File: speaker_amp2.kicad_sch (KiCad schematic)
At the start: 1 part

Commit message: refactored repo
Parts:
- removed MCU1: ESP32-C6-DevKit-N8, RF_Module:ESP32-C6-DevKit-N8, symbol RF_Module:ESP32-C6-DevKit-N8
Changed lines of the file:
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@@
 	(generator_version "8.0")
 	(paper "A4")
-	(symbol
-		(lib_id "RF_Module:ESP32-C6-DevKit-N8")
-		(at 93.98 91.44 0)
-		(unit 1)
-		(exclude_from_sim no)
-		(in_bom yes)
-		(on_board yes)
-		(dnp no)
-		(fields_autoplaced yes)
-		(property "Reference" "MCU1"
-			(at 93.98 45.72 0)
-			(effects
-				(font
-					(size 1.27 1.27)
-				)
-			)
-		)
-		(property "Value" "ESP32-C6-DevKit-N8"
-			(at 93.98 48.26 0)
-			(effects
-				(font
-					(size 1.27 1.27)
-				)
-			)
-		)
-		(property "Footprint" "RF_Module:ESP32-C6-DevKit-N8"
-			(at 93.98 78.74 0)
-			(effects
-				(font
-					(size 1.27 1.27)
-				)
-				(hide yes)
-			)
-		)
-		(property "Datasheet" "https://www.waveshare.com/wiki/ESP32-C6-DEV-KIT-N8"
-			(at 93.726 44.196 0)
-			(effects
-				(font
-					(size 1.27 1.27)
-				)
-				(hide yes)
-			)
-		)
-		(property "Description" ""
-			(at 93.98 78.74 0)
-			(effects
-				(font
-					(size 1.27 1.27)
-				)
-				(hide yes)
-			)
-		)
-		(pin "7"
-		)
-		(pin "25"
-		)
-		(pin "32"
-		)
-		(pin "26"
-		)
-		(pin "31"
-		)
-		(pin "30"
-		)
-		(pin "14"
-		)
-		(pin "21"
-		)
-		(pin "10"
-		)
-		(pin "19"
-		)
-		(pin "12"
-		)
-		(pin "27"
-		)
-		(pin "8"
-		)
-		(pin "20"
-		)
-		(pin "11"
-		)
-		(pin "16"
-		)
-		(pin "2"
-		)
-		(pin "4"
-		)
-		(pin "5"
-		)
-		(pin "3"
-		)
-		(pin "28"
-		)
-		(pin "23"
-		)
-		(pin "29"
-		)
-		(pin "24"
-		)
-		(pin "17"
-		)
-		(pin "15"
-		)
-		(pin "18"
-		)
-		(pin "13"
-		)
-		(pin "9"
-		)
-		(pin "22"
-		)
-		(pin "6"
-		)
-		(pin "1"
-		)
-		(instances
-			(project ""
-				(path "/2f0da60f-7f2b-417d-9b6a-7955d19177ea"
-					(reference "MCU1")
-					(unit 1)
-				)
-			)
-		)
-	)
 	(sheet_instances
 		(path "/"

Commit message: added mcu to schematic
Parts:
- added MCU1: ESP32-C6-DevKit-N8, Speaker Amp Lib:ESP32-C6-DevKit-N8, symbol Speaker Amp Lib:ESP32-C6-DevKit-N8
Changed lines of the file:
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@@
 	(generator_version "8.0")
 	(paper "A4")
+	(symbol
+		(lib_id "Speaker Amp Lib:ESP32-C6-DevKit-N8")
+		(at 83.82 93.98 0)
+		(unit 1)
+		(exclude_from_sim no)
+		(in_bom yes)
+		(on_board yes)
+		(dnp no)
+		(fields_autoplaced yes)
+		(property "Reference" "MCU1"
+			(at 83.82 48.26 0)
+			(effects
+				(font
+					(size 1.27 1.27)
+				)
+			)
+		)
+		(property "Value" "ESP32-C6-DevKit-N8"
+			(at 83.82 50.8 0)
+			(effects
+				(font
+					(size 1.27 1.27)
+				)
+			)
+		)
+		(property "Footprint" "Speaker Amp Lib:ESP32-C6-DevKit-N8"
+			(at 83.82 81.28 0)
+			(effects
+				(font
+					(size 1.27 1.27)
+				)
+				(hide yes)
+			)
+		)
+		(property "Datasheet" "https://www.waveshare.com/wiki/ESP32-C6-DEV-KIT-N8"
+			(at 83.566 46.736 0)
+			(effects
+				(font
+					(size 1.27 1.27)
+				)
+				(hide yes)
+			)
+		)
+		(property "Description" ""
+			(at 83.82 81.28 0)
+			(effects
+				(font
+					(size 1.27 1.27)
+				)
+				(hide yes)
+			)
+		)
+		(pin "22"
+		)
+		(pin "18"
+		)
+		(pin "9"
+		)
+		(pin "11"
+		)
+		(pin "27"
+		)
+		(pin "29"
+		)
+		(pin "17"
+		)
+		(pin "6"
+		)
+		(pin "19"
+		)
+		(pin "15"
+		)
+		(pin "16"
+		)
+		(pin "5"
+		)
+		(pin "8"
+		)
+		(pin "4"
+		)
+		(pin "1"
+		)
+		(pin "10"
+		)
+		(pin "12"
+		)
+		(pin "23"
+		)
+		(pin "14"
+		)
+		(pin "3"
+		)
+		(pin "7"
+		)
+		(pin "24"
+		)
+		(pin "28"
+		)
+		(pin "21"
+		)
+		(pin "25"
+		)
+		(pin "2"
+		)
+		(pin "30"
+		)
+		(pin "26"
+		)
+		(pin "32"
+		)
+		(pin "31"
+		)
+		(pin "20"
+		)
+		(pin "13"
+		)
+		(instances
+			(project ""
+				(path "/2f0da60f-7f2b-417d-9b6a-7955d19177ea"
+					(reference "MCU1")
+					(unit 1)
+				)
+			)
+		)
+	)
 	(sheet_instances
 		(path "/"

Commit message: added class D amp and datasheets, added most capacitors to schematic
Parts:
- added C1, C2, C3, C4: 0.47u, Capacitor_SMD:C_0805_2012Metric_Pad1.18x1.45mm_HandSolder, symbol Device:C
- added C10, C7, C9: 0.1u, Capacitor_SMD:C_0805_2012Metric_Pad1.18x1.45mm_HandSolder, symbol Device:C
- added C11, C12: 22u, Capacitor_SMD:C_1210_3225Metric_Pad1.33x2.70mm_HandSolder, symbol Device:C
- added C13, C14: 390u, Capacitor_THT:CP_Radial_D8.0mm_P3.50mm, symbol Device:C_Polarized
- added C5, C6: 1u, Capacitor_SMD:C_0805_2012Metric_Pad1.18x1.45mm_HandSolder, symbol Device:C
- added C8: 4.7u, Capacitor_SMD:C_0805_2012Metric_Pad1.18x1.45mm_HandSolder, symbol Device:C
- added U1: TAS5822MDCPR, DCP0038A-IPC_A, symbol Speaker Amp Lib:TAS5822MDCPR
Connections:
- new net: C1.1, U1.4 (BST_A+)
- new net: C1.2, U1.5 (OUT_A+)
- new net: C2.1, U1.1 (BST_A-)
- new net: C2.2, U1.2 (OUT_A-)
- new net: C5.2, U1.30 (AVDD)
- new net: C7.2, C8.2, U1.9 (DVDD)
- new net: C6.2, U1.11 (VR_DIG)
- new net: C3.2, U1.34 (OUT_B+)
- new net: C3.1, U1.35 (BST_B+)
- new net: C4.2, U1.37 (OUT_B-)
- new net: C4.1, U1.38 (BST_B-)
- new net GND: C10.1, C11.1, C12.1, C13.2, C14.2, C5.1, C6.1, C7.1, C8.1, C9.1, U1.12 (DGND), U1.3 (PGND), U1.31 (AGND), U1.36 (PGND), U1.39 (Thermal_Pad), U1.8 (DGND)
- new net PVDD: C10.2, C11.2, C12.2, C13.1, C14.1, C9.2, U1.32 (PVDD), U1.33 (PVDD), U1.6 (PVDD), U1.7 (PVDD)
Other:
- moved on the sheet: MCU1

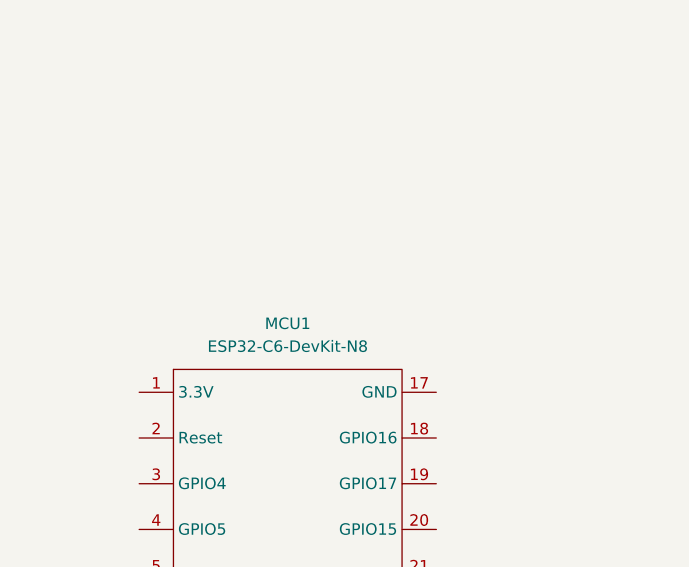
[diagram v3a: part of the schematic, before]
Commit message: added dcdc converter
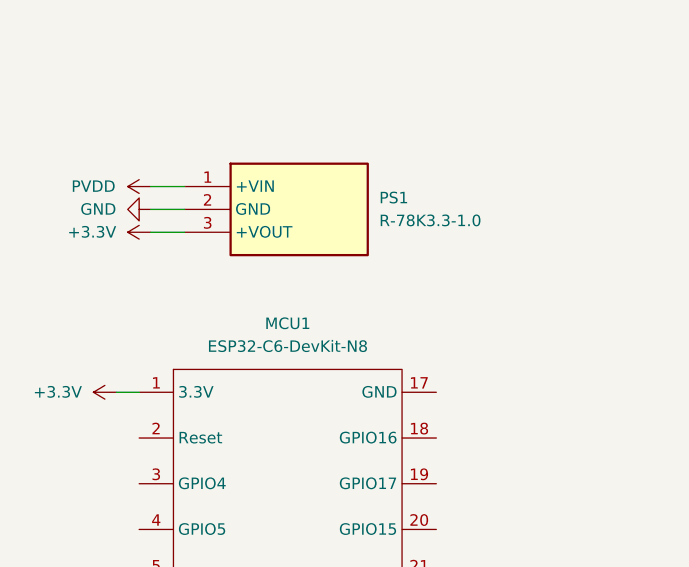
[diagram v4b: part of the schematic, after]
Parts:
- added PS1: R-78K3.3-1.0, Speaker Amp Lib:R78K3310, symbol Speaker Amp Lib:R-78K3.3-1.0
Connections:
- net GND: now also PS1.2 (GND)
- net PVDD: now also PS1.1 (+VIN)
- net +3.3V: now reaches MCU1.1 (3.3V)
- net +3.3V: now also PS1.3 (+VOUT)

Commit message: finalized logic level dcdc converter
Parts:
- added C15, C16: 10u, Capacitor_SMD:C_0805_2012Metric_Pad1.18x1.45mm_HandSolder, symbol Device:C
- added C17: 1n, Capacitor_SMD:C_0805_2012Metric_Pad1.18x1.45mm_HandSolder, symbol Device:C
- added L1: 100u, Speaker Amp Lib:RLS186, symbol Device:L
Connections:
- net +3.3V: now also C17.1
- net GND: now also C15.1, C16.1
- net PVDD: now also C15.2, L1.1; no longer PS1.1 (+VIN)
- new net: C16.2, C17.2, L1.2, PS1.1 (+VIN)
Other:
- moved on the sheet: MCU1, PS1

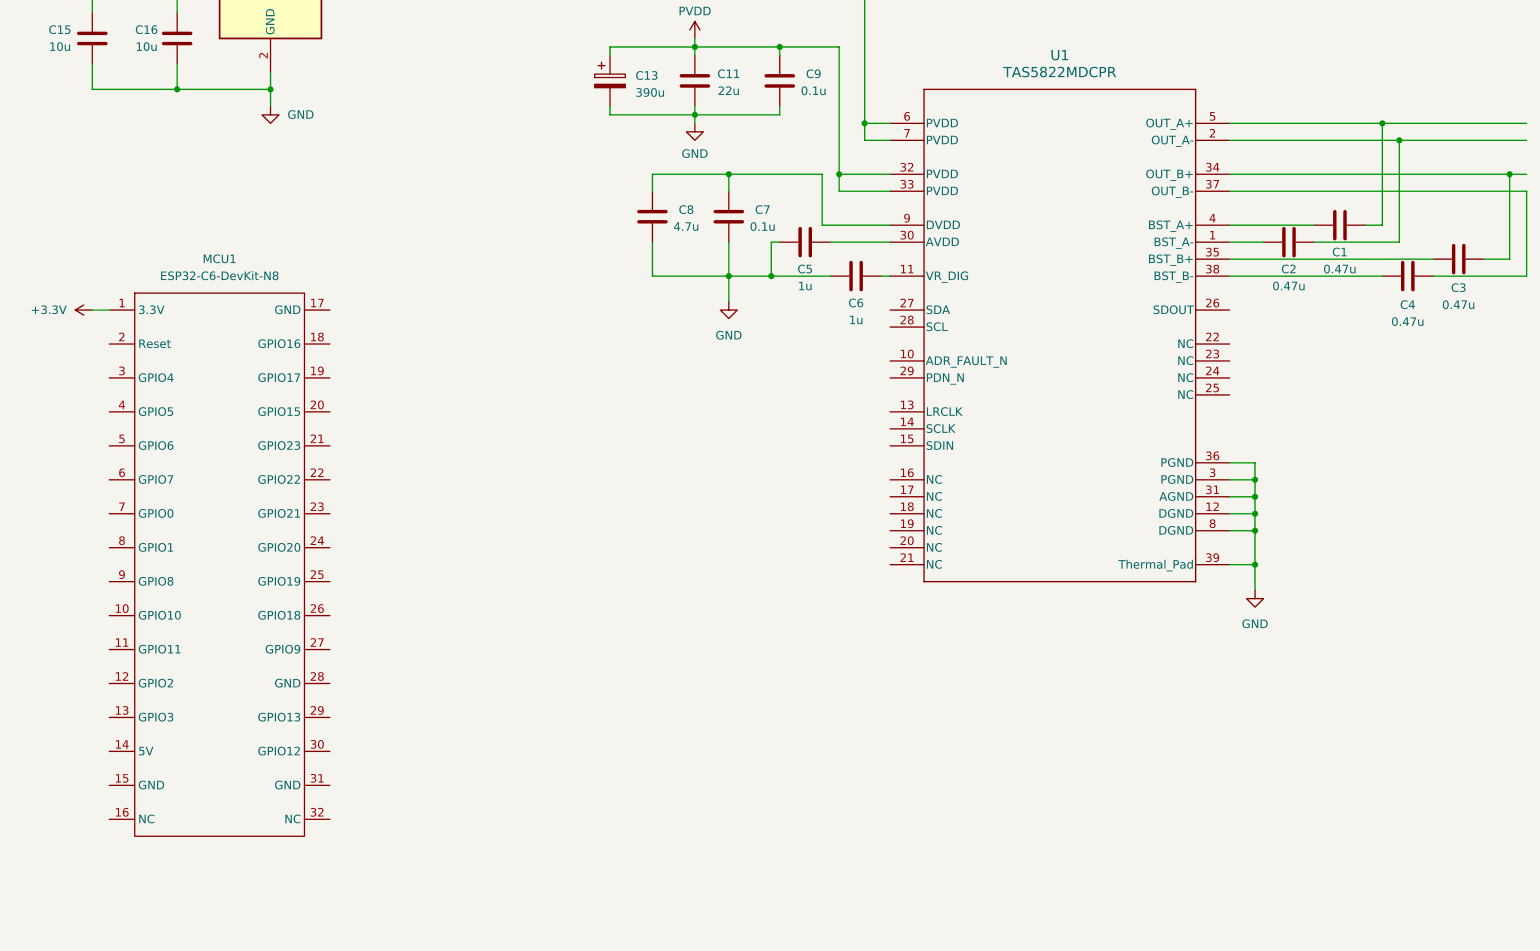
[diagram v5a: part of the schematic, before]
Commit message: replaced ESP32-C6 with ESP32-WROOM-32E
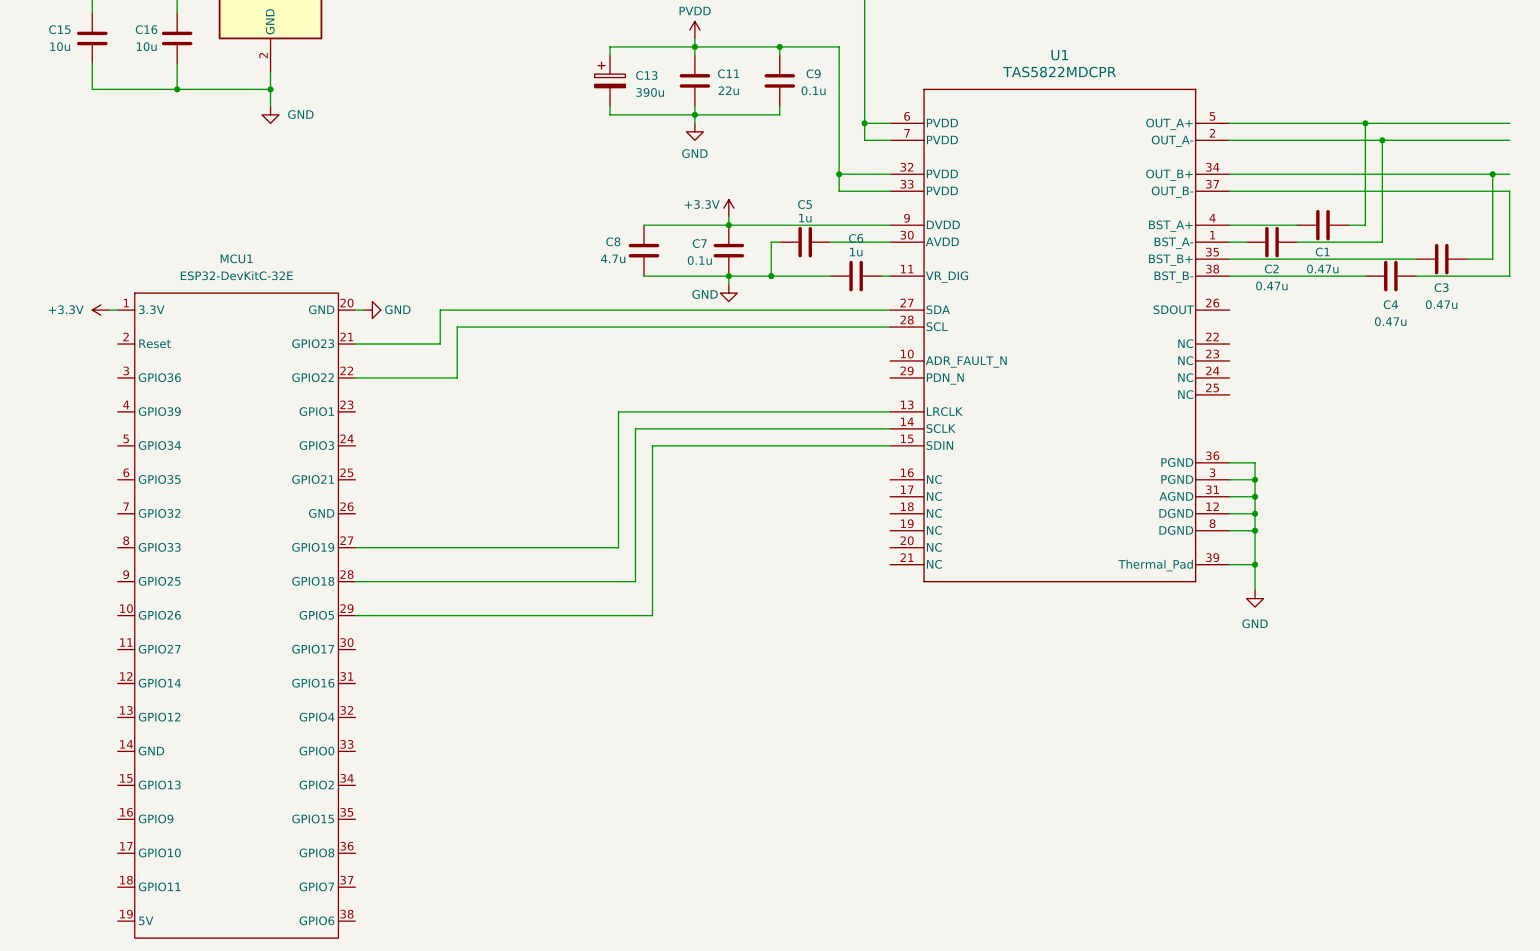
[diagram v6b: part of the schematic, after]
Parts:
- removed MCU1: ESP32-C6-DevKit-N8, Speaker Amp Lib:ESP32-C6-DevKit-N8, symbol Speaker Amp Lib:ESP32-C6-DevKit-N8
- added MCU1: ESP32-DevKitC-32E, Speaker Amp Lib:ESP32-DevKitC-32E, symbol Speaker Amp Lib:ESP32-DevKitC-32E
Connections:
- net +3.3V: now also C7.2, C8.2, U1.9 (DVDD), MCU1.1 (3.3V)
- net GND: now also MCU1.20 (GND)
- net at U1.13 (LRCLK): now also MCU1.27 (GPIO19)
- net at U1.14 (SCLK): now also MCU1.28 (GPIO18)
- net at U1.15 (SDIN): now also MCU1.29 (GPIO5)
- net at U1.27 (SDA): now also MCU1.21 (GPIO23)
- net at U1.28 (SCL): now also MCU1.22 (GPIO22)
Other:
- moved on the sheet: C1, C2, C3, C4, C7, C8

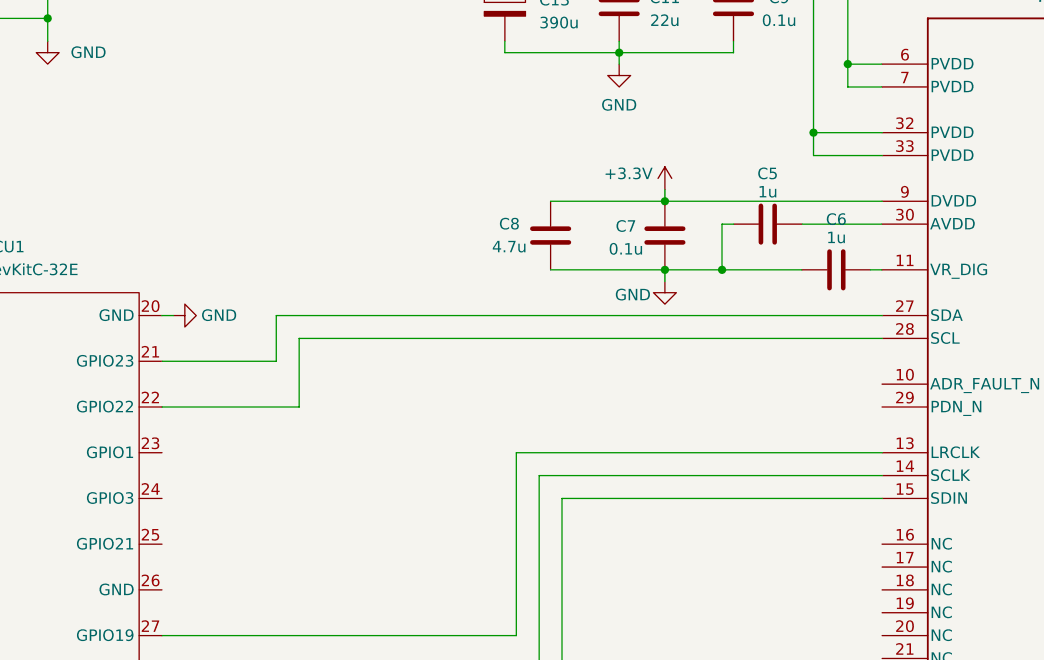
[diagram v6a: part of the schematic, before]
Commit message: added communication wires with amp
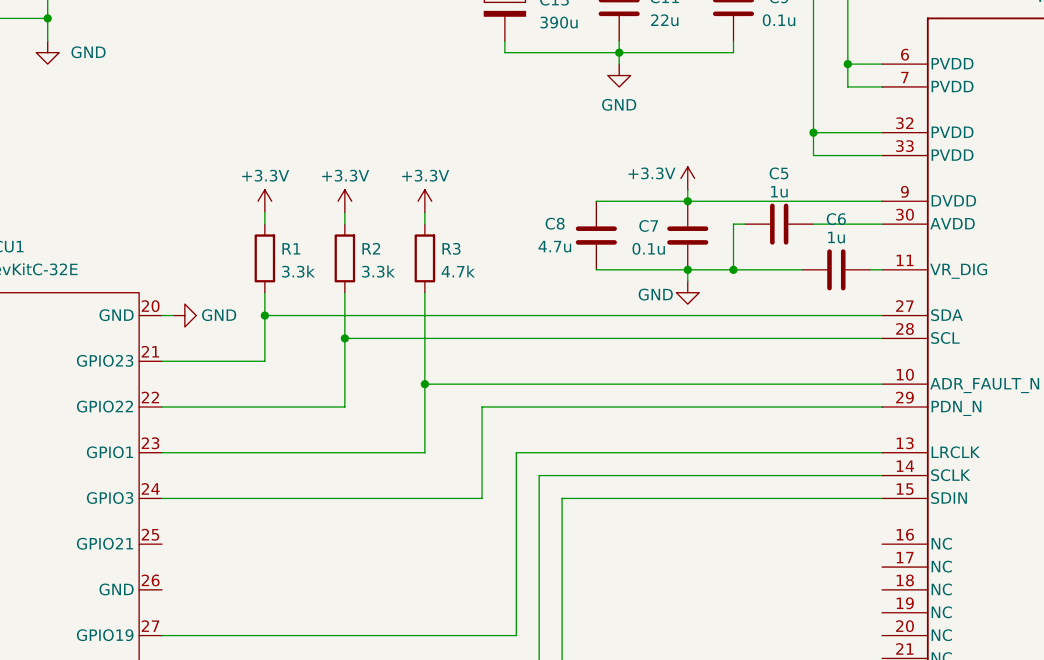
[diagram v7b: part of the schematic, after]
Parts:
- added R1, R2: 3.3k, Resistor_SMD:R_0805_2012Metric_Pad1.20x1.40mm_HandSolder, symbol Device:R
- added R3: 4.7k, Resistor_SMD:R_0805_2012Metric_Pad1.20x1.40mm_HandSolder, symbol Device:R
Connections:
- net +3.3V: now also R1.2, R2.2, R3.2
- net at U1.10 (ADR_FAULT_N): now also MCU1.23 (GPIO1), R3.1
- net at MCU1.21 (GPIO23), U1.27 (SDA): now also R1.1
- net at MCU1.22 (GPIO22), U1.28 (SCL): now also R2.1
- net at U1.29 (PDN_N): now also MCU1.24 (GPIO3)
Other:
- moved on the sheet: C5, C7, C8
